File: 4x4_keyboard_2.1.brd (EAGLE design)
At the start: 72 x 134.4 mm, 82 parts, among them U2 AMS1117-5.0

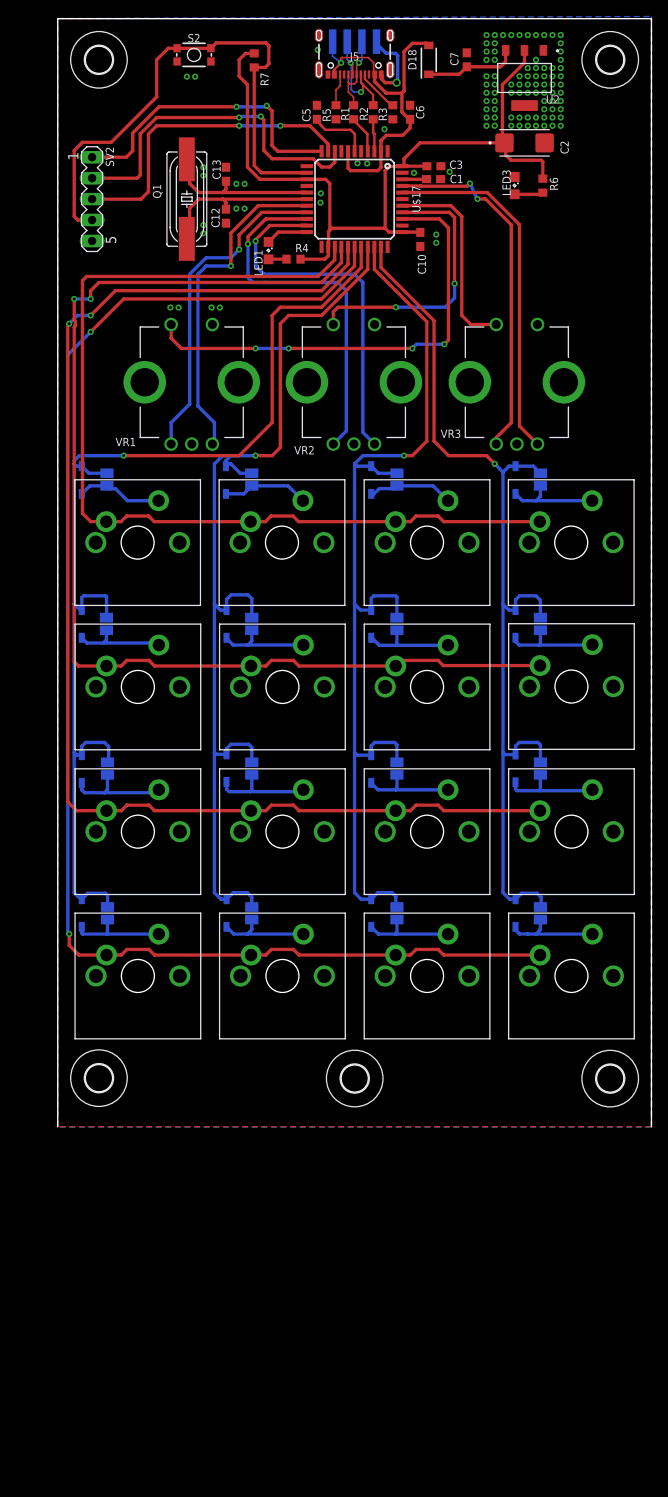
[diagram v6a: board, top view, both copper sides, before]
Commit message: delete the scale parameters
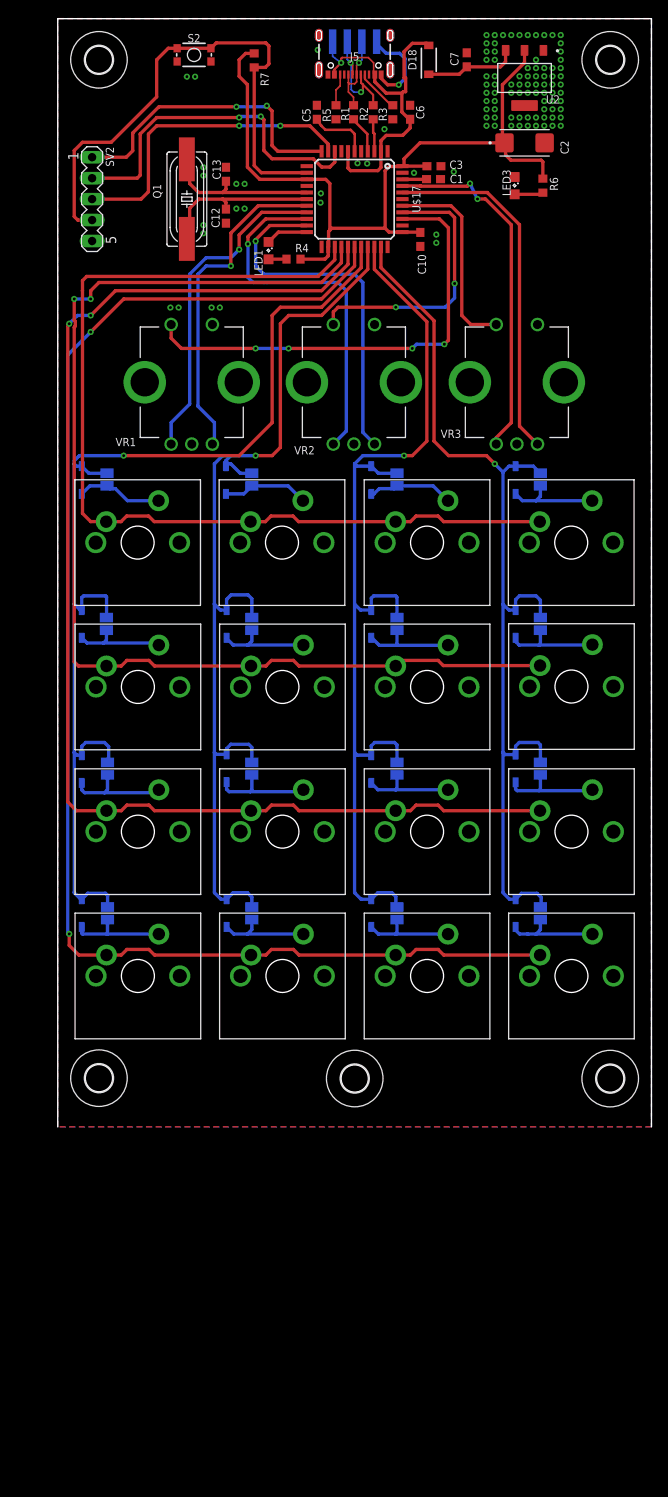
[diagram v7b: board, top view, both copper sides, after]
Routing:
- net GND: track 9.35 -> 10.4 mm
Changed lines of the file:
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@@
 <wire x1="77" y1="164.992" x2="5" y2="164.992" width="0" layer="20"/>
 <wire x1="5" y1="164.992" x2="5" y2="30.59" width="0" layer="20"/>
-<dimension x1="57.404" y1="94.234" x2="59.69" y2="94.234" x3="58.547" y3="24.623" textsize="1.778" layer="1" dtype="horizontal" precision="6"/>
-<dimension x1="7.747" y1="93.853" x2="7.874" y2="91.567" x3="89.789" y3="92.71" textsize="1.778" layer="1" dtype="vertical" precision="6"/>
-<dimension x1="12.7" y1="76.327" x2="12.573" y2="74.041" x3="90.932" y3="75.184" textsize="1.778" layer="1" dtype="vertical" precision="6"/>
-<dimension x1="9.271" y1="58.801" x2="9.017" y2="56.515" x3="97.536" y3="57.658" textsize="1.778" layer="1" dtype="vertical" precision="6"/>
 </plain>
 <attributes>
@@
 <polygon width="0.4064" layer="16">
 <vertex x="5" y="165"/>
-<vertex x="77" y="165.254"/>
+<vertex x="77" y="165"/>
 <vertex x="77" y="30.59"/>
 <vertex x="5" y="30.59"/>
@@
 <via x="41.36" y="147.466" extent="1-16" drill="0.35"/>
 <via x="42.524" y="147.421" extent="1-16" drill="0.35"/>
-<via x="52.524" y="146.421" extent="1-16" drill="0.35"/>
+<via x="53.032" y="146.421" extent="1-16" drill="0.35"/>
 <via x="48.206" y="146.294" extent="1-16" drill="0.35"/>
 <via x="36.909" y="143.804" extent="1-16" drill="0.35"/>
@@
 <via x="22.661" y="146.956" extent="1-16" drill="0.35"/>
 <wire x1="43.667" y1="162.207" x2="43.667" y2="161.946" width="0.4064" layer="16"/>
-<wire x1="43.667" y1="161.946" x2="44.831" y2="160.782" width="0.4064" layer="16"/>
-<wire x1="44.831" y1="160.782" x2="45.974" y2="160.782" width="0.4064" layer="16"/>
-<wire x1="45.974" y1="160.782" x2="46.228" y2="160.528" width="0.4064" layer="16"/>
-<wire x1="46.228" y1="160.528" x2="46.228" y2="157.353" width="0.4064" layer="16"/>
-<wire x1="46.228" y1="157.353" x2="46.101" y2="157.226" width="0.4064" layer="16"/>
-<via x="46.101" y="157.226" extent="1-16" drill="0.6"/>
-<wire x1="46.101" y1="157.226" x2="44.704" y2="157.226" width="0.4064" layer="1"/>
-<wire x1="44.704" y1="157.226" x2="44.323" y2="157.607" width="0.4064" layer="1"/>
-<wire x1="44.323" y1="157.607" x2="44.323" y2="158.115" width="0.4064" layer="1"/>
-<wire x1="44.323" y1="158.115" x2="44.225" y2="158.213" width="0.4064" layer="1"/>
+<wire x1="44.831" y1="160.782" x2="43.667" y2="161.946" width="0.4064" layer="16"/>
 <polygon width="0.1524" layer="1" isolate="0.254" orphans="yes">
 <vertex x="5" y="165"/>
@@
 <vertex x="5" y="32"/>
 </polygon>
+<via x="46.355" y="156.972" extent="1-16" drill="0.35"/>
+<wire x1="45" y1="156.972" x2="46.355" y2="156.972" width="0.4064" layer="1"/>
+<wire x1="46.355" y1="156.972" x2="47.117" y2="157.734" width="0.4064" layer="16"/>
+<wire x1="46.482" y1="160.782" x2="44.831" y2="160.782" width="0.4064" layer="16"/>
+<wire x1="47.117" y1="157.734" x2="47.117" y2="160.147" width="0.4064" layer="16"/>
+<wire x1="47.117" y1="160.147" x2="46.482" y2="160.782" width="0.4064" layer="16"/>
+<wire x1="45" y1="156.972" x2="44.225" y2="157.747" width="0.4064" layer="1"/>
+<wire x1="44.225" y1="157.747" x2="44.225" y2="157.7738" width="0.4064" layer="1"/>
 </signal>
 <signal name="D-">
@@
 <wire x1="43.307" y1="159.639" x2="42.672" y2="160.274" width="0.2" layer="1"/>
 <wire x1="38.55" y1="158.213" x2="38.55" y2="158.692" width="0.2" layer="1"/>
-<wire x1="44.2" y1="148.907" x2="44.2" y2="150.2" width="0.4064" layer="1"/>
+<wire x1="44.2" y1="150.2" x2="44.2" y2="148.907" width="0.4064" layer="1"/>
 <wire x1="44.842625" y1="150.842625" x2="44.2" y2="150.2" width="0.4064" layer="1"/>
 <wire x1="47.735" y1="152.7885" x2="47.735" y2="152.781" width="0.4064" layer="1"/>
@@
 <wire x1="46.736" y1="153.67" x2="47.625" y2="152.781" width="0.4064" layer="1"/>
 <wire x1="47.625" y1="152.781" x2="47.735" y2="152.781" width="0.4064" layer="1"/>
-<wire x1="47" y1="161" x2="48" y2="162" width="0.4064" layer="1"/>
+<wire x1="48" y1="162" x2="47" y2="161" width="0.4064" layer="1"/>
 <wire x1="48" y1="162" x2="49.75" y2="162" width="0.4064" layer="1"/>
 <wire x1="49.75" y1="162" x2="50" y2="161.75" width="0.4064" layer="1"/>
@@
 <wire x1="43.45" y1="157.337" x2="44.831" y2="155.956" width="0.4064" layer="1"/>
 <wire x1="44.831" y1="155.956" x2="46.736" y2="155.956" width="0.4064" layer="1"/>
-<wire x1="47" y1="161" x2="47" y2="156.22" width="0.4064" layer="1"/>
-<wire x1="47" y1="156.22" x2="46.736" y2="155.956" width="0.4064" layer="1"/>
 <wire x1="39.37" y1="159.639" x2="39.37" y2="160.147" width="0.254" layer="1"/>
 <wire x1="39.37" y1="160.147" x2="39.497" y2="160.274" width="0.254" layer="1"/>
 <wire x1="38.55" y1="158.692" x2="38.55" y2="158.819" width="0.254" layer="1"/>
 <wire x1="38.55" y1="158.819" x2="39.37" y2="159.639" width="0.254" layer="1"/>
+<wire x1="47" y1="161" x2="47" y2="157.8074" width="0.4064" layer="1"/>
+<wire x1="47" y1="157.8074" x2="47.1904" y2="157.8074" width="0.4064" layer="1"/>
+<wire x1="47.1904" y1="157.8074" x2="47.1904" y2="156.1366" width="0.4064" layer="1"/>
+<wire x1="47.1904" y1="156.1366" x2="46.9166" y2="156.1366" width="0.4064" layer="1"/>
+<wire x1="46.9166" y1="156.1366" x2="46.736" y2="155.956" width="0.4064" layer="1"/>
 </signal>
 <signal name="VCC">
@@
 <wire x1="40.594765625" y1="159.557234375" x2="40.594765625" y2="156.382234375" width="0.2" layer="16"/>
 <wire x1="40.894" y1="156.083" x2="41.783" y2="156.083" width="0.2" layer="16"/>
-<wire x1="40.894" y1="156.083" x2="40.594765625" y2="156.382234375" width="0.2" layer="16"/>
+<wire x1="40.594765625" y1="156.382234375" x2="40.894" y2="156.083" width="0.2" layer="16"/>
 <via x="41.783" y="156.083" extent="1-16" drill="0.35"/>
 <wire x1="40.513" y1="159.639" x2="40.767" y2="159.385" width="0.2" layer="1"/>

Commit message: added log
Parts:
- added U$18: (no value), SparkFun-Aesthetics:SMART_BASIC_LOGO
- moved R6 1.00 mm to (62.8, 144.7)
- renumbered J5 to USB_C
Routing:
- net VCC: track 97.1 -> 96.1 mm
- net N$11: track 3.50 -> 2.50 mm
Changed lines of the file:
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@@
 <drawing>
 <settings>
-<setting alwaysvectorfont="no"/>
+<setting alwaysvectorfont="yes"/>
 <setting keepoldvectorfont="yes"/>
 <setting verticaltext="up"/>
@@
 <attribute name="MF" value="AVX Interconnect / Elco" x="142.89" y="75" size="1.778" layer="27" display="off"/>
 <attribute name="MP" value="TAJC226K025RNJ" x="142.89" y="75" size="1.778" layer="27" display="off"/>
-<attribute name="NAME" x="65.97" y="150.2" size="1" layer="25" rot="R270"/>
+<attribute name="NAME" x="55.97" y="149.2" size="1" layer="25" rot="R270"/>
 <attribute name="PACKAGE" value="2312 AVX Interconnect / Elco" x="142.89" y="75" size="1.778" layer="27" display="off"/>
 <attribute name="PRICE" value="None" x="142.89" y="75" size="1.778" layer="27" display="off"/>
@@
 </element>
 <element name="LED3" library="led" package="SML0805" value="" x="60.41" y="144.74" smashed="yes" rot="R270">
-<attribute name="NAME" x="58.934" y="146.684" size="1" layer="25" rot="R270"/>
+<attribute name="NAME" x="59.066" y="144.316" size="1" layer="25" rot="R90"/>
 <attribute name="VALUE" x="58.41" y="146.24" size="1.27" layer="27" rot="R270"/>
 </element>
@@
 </element>
 <element name="R4" library="audio amplifier example" package="R0603" value="1K" x="33.593" y="135.83" smashed="yes" rot="R180">
-<attribute name="NAME" x="33.804" y="136.678" size="1" layer="25"/>
+<attribute name="NAME" x="32.804" y="136.678" size="1" layer="25"/>
 <attribute name="VALUE" x="34.482" y="137.862" size="1" layer="27" rot="R180"/>
 </element>
-<element name="R6" library="audio amplifier example" package="R0603" value="1K" x="63.83" y="144.74" smashed="yes" rot="R90">
-<attribute name="NAME" x="64.678" y="145.768" size="1" layer="25" rot="R270"/>
-<attribute name="VALUE" x="65.862" y="143.851" size="1" layer="27" rot="R90"/>
+<element name="R6" library="audio amplifier example" package="R0603" value="1K" x="62.83" y="144.74" smashed="yes" rot="R90">
+<attribute name="NAME" x="62.408" y="143.085" size="1" layer="25" rot="R270"/>
+<attribute name="VALUE" x="64.862" y="143.851" size="1" layer="27" rot="R90"/>
 </element>
 <element name="R7" library="audio amplifier example" package="R0603" value="1K" x="28.83" y="159.93" smashed="yes" rot="R90">
@@
 <element name="U$16" library="cherrymx" package="CHERRY-MX" value="CHERRY-MX" x="67.3" y="48.9" locked="yes" smashed="yes"/>
 <element name="U$17" library="SparkFun-IC-Microcontroller" package="TQFP44" value="32U4" x="41" y="143.107" smashed="yes" rot="R270">
-<attribute name="NAME" x="47.985" y="143.107" size="1" layer="25" font="vector" ratio="11" rot="R270" align="bottom-center"/>
+<attribute name="NAME" x="45.985" y="136.107" size="1" layer="25" font="vector" ratio="11" rot="R270" align="bottom-center"/>
 <attribute name="PROD_ID" value="IC-11161" x="11.79" y="122.787" size="1.778" layer="27" rot="R270" display="off"/>
 <attribute name="VALUE" x="33.38" y="143.107" size="1" layer="27" font="vector" ratio="11" rot="R270" align="bottom-center"/>
@@
 </element>
 <element name="JP14" library="SparkFun-Connectors" package="USB-SOLDER-PADS" value="USB_SOLDER_PADS" x="41" y="162.207" smashed="yes" rot="MR270"/>
-<element name="J5" library="USBC" package="USB-C-16P-5" value="" x="41" y="157.873" smashed="yes" rot="R180">
-<attribute name="NAME" x="41" y="160.413" size="1" layer="25" rot="R180" align="center"/>
+<element name="USB_C" library="USBC" package="USB-C-16P-5" value="" x="41" y="157.873" smashed="yes" rot="R180">
+<attribute name="NAME" x="34.587" y="160.904" size="1" layer="25" rot="R270" align="center"/>
 <attribute name="VALUE" x="41" y="161.683" size="0.762" layer="27" rot="R180" align="center"/>
 </element>
@@
 <attribute name="POPULARITY" value="3" x="41.016" y="36.463" size="1.778" layer="27" display="off"/>
 </element>
+<element name="U$18" library="SparkFun-Aesthetics" library_urn="urn:adsk.eagle:library:507" package="SMART_BASIC_LOGO" package3d_urn="urn:adsk.eagle:package:37157/1" value="" x="62" y="151" smashed="yes" rot="R270"/>
 </elements>
 <signals>
@@
 </polygon>
 <contactref element="JP14" pad="GND"/>
-<contactref element="J5" pad="GND"/>
-<contactref element="J5" pad="GND2"/>
+<contactref element="USB_C" pad="GND"/>
+<contactref element="USB_C" pad="GND2"/>
 <contactref element="R3" pad="2"/>
 <contactref element="R5" pad="2"/>
@@
 <contactref element="D18" pad="2"/>
 <contactref element="JP14" pad="VBUS"/>
-<contactref element="J5" pad="VBUS1"/>
-<contactref element="J5" pad="VBUS2"/>
+<contactref element="USB_C" pad="VBUS1"/>
+<contactref element="USB_C" pad="VBUS2"/>
 <wire x1="40.2" y1="148.907" x2="40.2" y2="146.871" width="0.4064" layer="1"/>
 <wire x1="40.2" y1="146.871" x2="40.513" y2="146.558" width="0.4064" layer="1"/>
@@
 <wire x1="58.928" y1="156.972" x2="58.928" y2="150.177" width="0.4064" layer="1"/>
 <wire x1="58.928" y1="150.177" x2="59.175" y2="149.93" width="0.4064" layer="1"/>
-<wire x1="63.83" y1="145.59" x2="63.83" y2="147.625" width="0.4064" layer="1"/>
-<wire x1="63.83" y1="147.625" x2="63.627" y2="147.828" width="0.4064" layer="1"/>
-<wire x1="63.627" y1="147.828" x2="59.944" y2="147.828" width="0.4064" layer="1"/>
+<wire x1="62.83" y1="145.59" x2="62.83" y2="147.625" width="0.4064" layer="1"/>
+<wire x1="62.83" y1="147.625" x2="62.627" y2="147.828" width="0.4064" layer="1"/>
+<wire x1="62.627" y1="147.828" x2="59.944" y2="147.828" width="0.4064" layer="1"/>
 <wire x1="59.944" y1="147.828" x2="59.309" y2="148.463" width="0.4064" layer="1"/>
 <wire x1="59.309" y1="148.463" x2="59.309" y2="149.796" width="0.4064" layer="1"/>
@@
 <contactref element="R6" pad="1"/>
 <contactref element="LED3" pad="A"/>
-<wire x1="60.41" y1="143.69" x2="63.63" y2="143.69" width="0.4064" layer="1"/>
-<wire x1="63.63" y1="143.69" x2="63.83" y2="143.89" width="0.4064" layer="1"/>
+<wire x1="60.41" y1="143.69" x2="62.63" y2="143.69" width="0.4064" layer="1"/>
+<wire x1="62.63" y1="143.69" x2="62.83" y2="143.89" width="0.4064" layer="1"/>
 </signal>
 <signal name="N$4">
@@
 <signal name="D-_HV">
 <contactref element="JP14" pad="D-"/>
-<contactref element="J5" pad="B7"/>
-<contactref element="J5" pad="A7"/>
+<contactref element="USB_C" pad="B7"/>
+<contactref element="USB_C" pad="A7"/>
 <contactref element="R2" pad="2"/>
 <wire x1="41.783" y1="158.18" x2="41.783" y2="157.226" width="0.254" layer="1"/>
@@
 <signal name="DP_HV">
 <contactref element="JP14" pad="D+"/>
-<contactref element="J5" pad="A6"/>
-<contactref element="J5" pad="B6"/>
+<contactref element="USB_C" pad="A6"/>
+<contactref element="USB_C" pad="B6"/>
 <contactref element="R1" pad="2"/>
 <wire x1="41.25" y1="159.36" x2="41.25" y2="158.213" width="0.2" layer="1"/>
@@
 </signal>
 <signal name="N$7">
-<contactref element="J5" pad="A5"/>
+<contactref element="USB_C" pad="A5"/>
 <contactref element="R3" pad="1"/>
 <wire x1="42.25" y1="158.213" x2="42.25" y2="157.66786875" width="0.254" layer="1"/>
@@
 </signal>
 <signal name="N$13">
-<contactref element="J5" pad="B5"/>
+<contactref element="USB_C" pad="B5"/>
 <contactref element="R5" pad="1"/>
 <wire x1="39.25" y1="156.852" x2="39.25" y2="158.213" width="0.2" layer="1"/>
@@
 </signals>
 <mfgpreviewcolors>
-<mfgpreviewcolor name="soldermaskcolor" color="0xC8008000"/>
-<mfgpreviewcolor name="silkscreencolor" color="0xFFFEFEFE"/>
-<mfgpreviewcolor name="backgroundcolor" color="0xFF282828"/>
+<mfgpreviewcolor name="soldermaskcolor" color="0xC8000000"/>
+<mfgpreviewcolor name="silkscreencolor" color="0xFFFFFFFF"/>
+<mfgpreviewcolor name="backgroundcolor" color="0xFFFFFFFF"/>
 <mfgpreviewcolor name="coppercolor" color="0xFFFFBF00"/>
 <mfgpreviewcolor name="substratecolor" color="0xFF786E46"/>
@@
 </board>
 </drawing>
+<compatibility>
+<note version="8.2" severity="warning">
+Since Version 8.2, EAGLE supports online libraries. The ids
+of those online libraries will not be understood (or retained)
+with this version.
+</note>
+<note version="8.3" severity="warning">
+Since Version 8.3, EAGLE supports URNs for individual library
+assets (packages, symbols, and devices). The URNs of those assets
+will not be understood (or retained) with this version.
+</note>
+<note version="8.3" severity="warning">
+Since Version 8.3, EAGLE supports the association of 3D packages
+with devices in libraries, schematics, and board files. Those 3D
+packages will not be understood (or retained) with this version.
+</note>
+</compatibility>
 </eagle>
